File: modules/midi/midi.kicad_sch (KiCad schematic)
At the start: 9 parts, among them J2 GATE_OUTS, J3 AudioJack3, J4 CONFIG

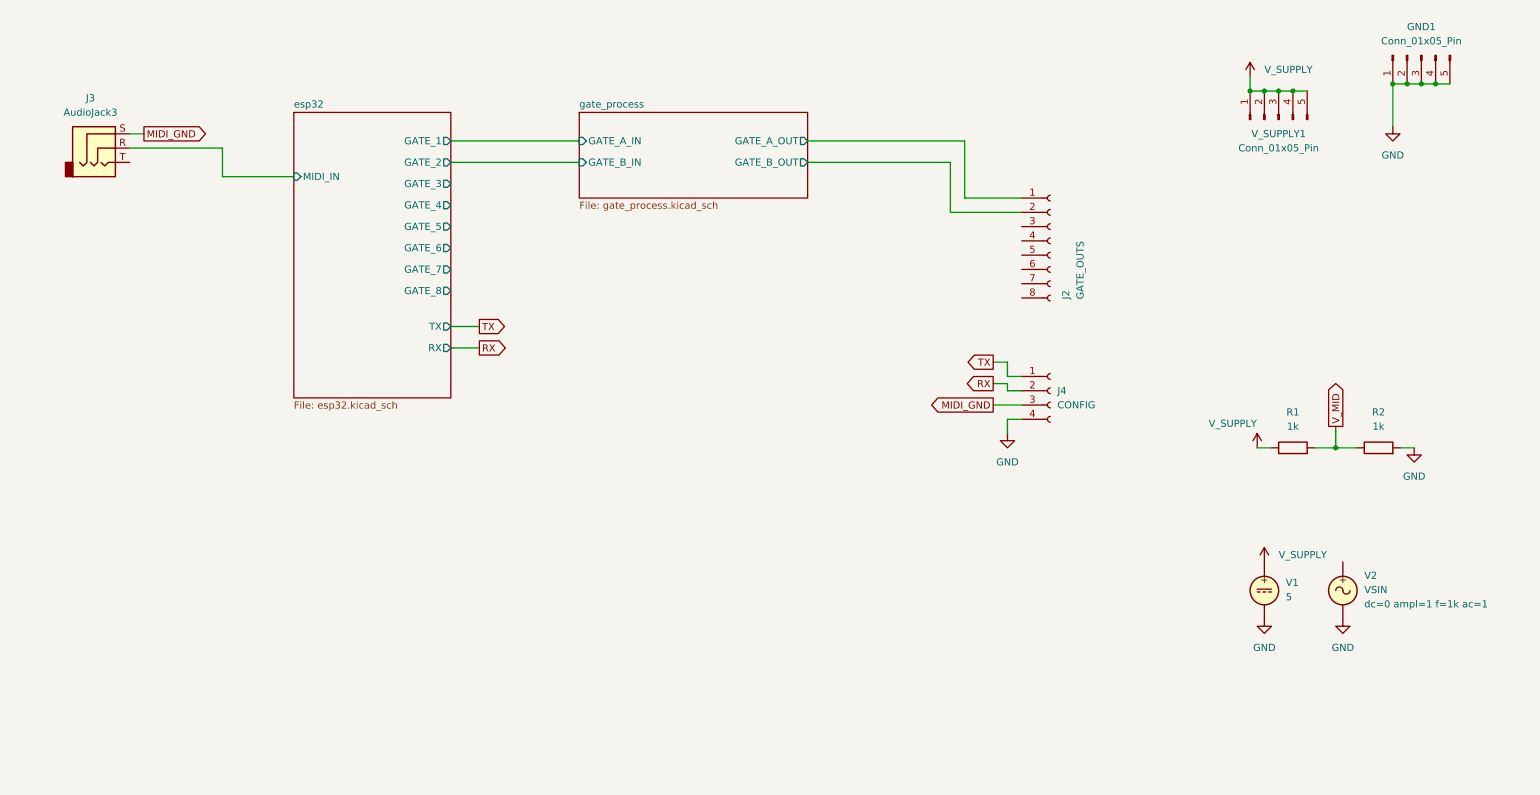
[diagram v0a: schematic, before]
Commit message: Add MIDI PCB
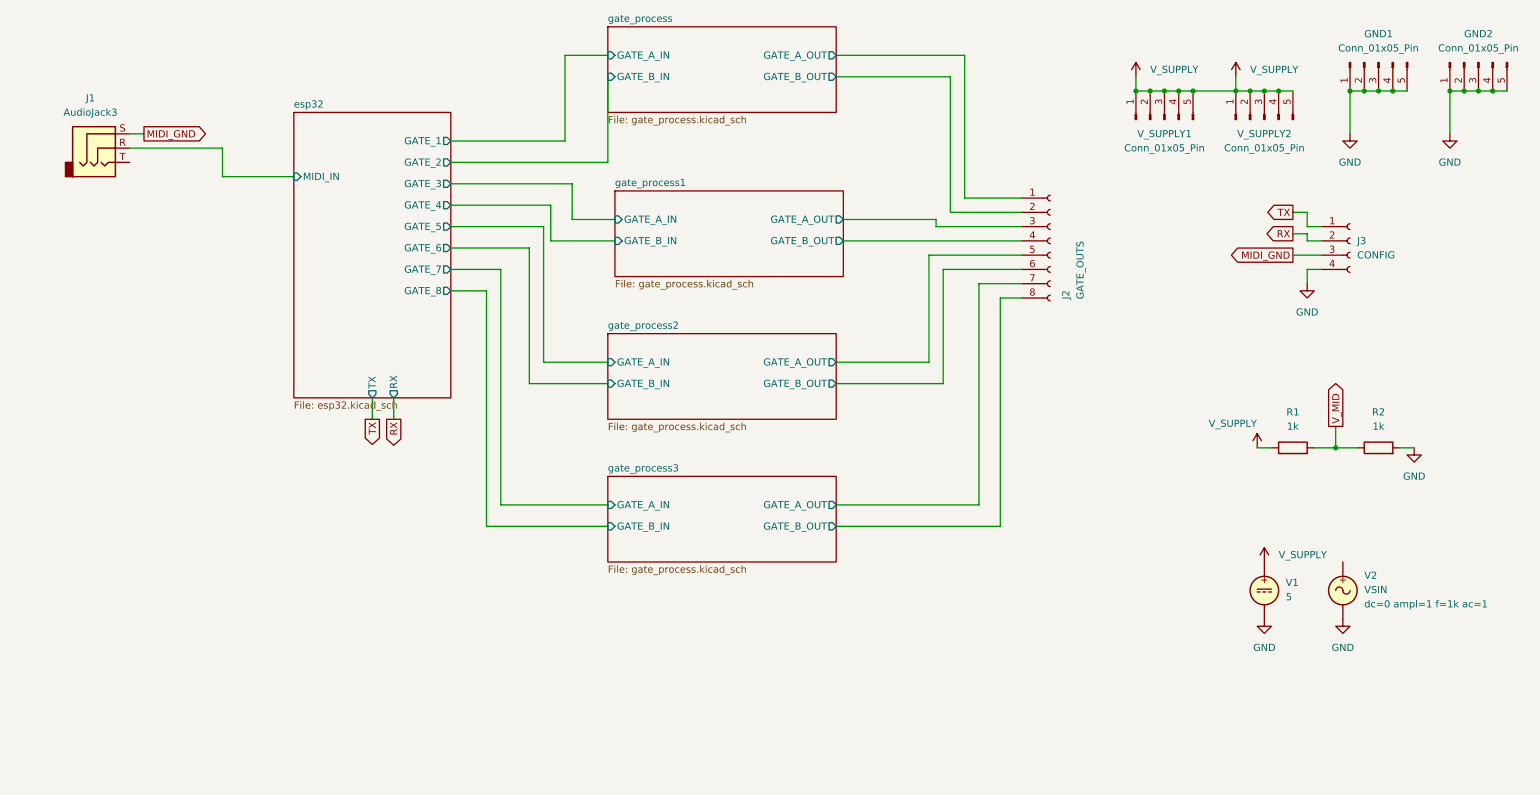
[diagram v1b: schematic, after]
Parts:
- added GND2, V_SUPPLY2: Conn_01x05_Pin, BreadModular_MISC:Power_Connector, symbol Connector:Conn_01x05_Pin
- renumbered J3 to J1, J4 to J3
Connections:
- net GND: now also GND2.1 (Pin_1), GND2.2 (Pin_2), GND2.3 (Pin_3), GND2.4 (Pin_4), GND2.5 (Pin_5)
- net V_SUPPLY: now also V_SUPPLY2.1 (Pin_1), V_SUPPLY2.2 (Pin_2), V_SUPPLY2.3 (Pin_3), V_SUPPLY2.4 (Pin_4), V_SUPPLY2.5 (Pin_5)
- net gate_process1/GATE_A_OUT: now reaches J2.3 (Pin_3)
- net gate_process1/GATE_B_OUT: now reaches J2.4 (Pin_4)
- net gate_process2/GATE_A_OUT: now reaches J2.5 (Pin_5)
- net gate_process2/GATE_B_OUT: now reaches J2.6 (Pin_6)
- net gate_process3/GATE_A_OUT: now reaches J2.7 (Pin_7)
- net gate_process3/GATE_B_OUT: now reaches J2.8 (Pin_8)
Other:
- added sheet gate_process1 (gate_process.kicad_sch)
- added sheet gate_process2 (gate_process.kicad_sch)
- added sheet gate_process3 (gate_process.kicad_sch)
- moved on the sheet: GND1, J3, V_SUPPLY1

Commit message: Implement the PCB layout and routing
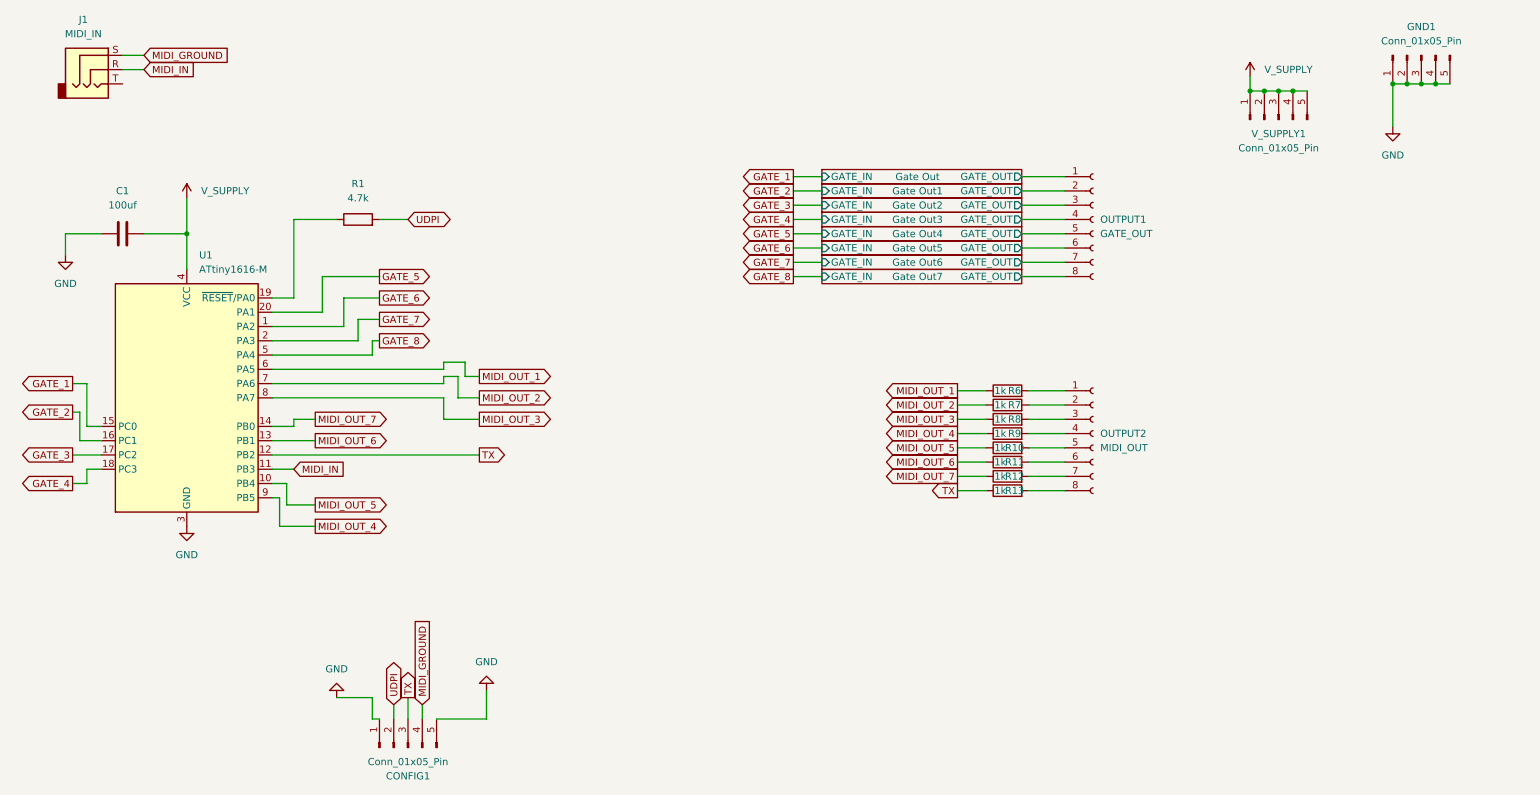
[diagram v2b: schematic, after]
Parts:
- removed GND2, V_SUPPLY2: Conn_01x05_Pin, BreadModular_MISC:Power_Connector, symbol Connector:Conn_01x05_Pin
- removed J2: GATE_OUTS, Connector_PinSocket_2.54mm:PinSocket_1x08_P2.54mm_Vertical, symbol Connector:Conn_01x08_Socket
- removed J3: CONFIG, Connector_PinSocket_2.54mm:PinSocket_1x04_P2.54mm_Vertical, symbol Connector:Conn_01x04_Socket
- removed R2: 1k, Resistor_SMD:R_0402_1005Metric, symbol Device:R
- removed V1: 5, symbol Simulation_SPICE:VDC
- removed V2: VSIN, symbol Simulation_SPICE:VSIN
- added C1: 100uf, Capacitor_SMD:C_1206_3216Metric, symbol Device:C
- added CONFIG1: Conn_01x05_Pin, BreadModular_MISC:Power_Connector, symbol Connector:Conn_01x05_Pin
- added OUTPUT1: GATE_OUT, Connector_PinSocket_2.54mm:PinSocket_1x08_P2.54mm_Vertical, symbol Connector:Conn_01x08_Socket
- added OUTPUT2: MIDI_OUT, Connector_PinSocket_2.54mm:PinSocket_1x08_P2.54mm_Vertical, symbol Connector:Conn_01x08_Socket
- added R10, R11, R12, R13, R6, R7, R8, R9: 1k, Resistor_SMD:R_0402_1005Metric, symbol Device:R
- added U1: ATtiny1616-M, Package_DFN_QFN:VQFN-20-1EP_3x3mm_P0.4mm_EP1.7x1.7mm, symbol MCU_Microchip_ATtiny:ATtiny1616-M
- J1: value AudioJack3 -> MIDI_IN
- R1: value 1k -> 4.7k
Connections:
- net GND: now also C1.1, CONFIG1.1 (Pin_1), CONFIG1.5 (Pin_5), U1.21 (GND), U1.3 (GND)
- net TX: now also CONFIG1.3 (Pin_3), R13.1, U1.12 (PB2)
- net V_SUPPLY: now also C1.2, U1.4 (VCC); no longer R1.1
- net MIDI_GND renamed MIDI_GROUND
- net MIDI_GROUND: now also CONFIG1.4 (Pin_4)
- net V_MID renamed UDPI
- net UDPI: now also CONFIG1.2 (Pin_2)
- net esp32/MIDI_IN renamed MIDI_IN
- net MIDI_IN: now also U1.11 (PB3)
- new net: OUTPUT2.1 (Pin_1), R6.2
- new net: OUTPUT2.2 (Pin_2), R7.2
- new net: OUTPUT2.3 (Pin_3), R8.2
- new net: OUTPUT2.4 (Pin_4), R9.2
- new net: OUTPUT2.5 (Pin_5), R10.2
- new net: OUTPUT2.6 (Pin_6), R11.2
- new net: OUTPUT2.7 (Pin_7), R12.2
- new net: OUTPUT2.8 (Pin_8), R13.2
- new net: R1.1, U1.19 (~{RESET}/PA0)
- new net GATE_1: U1.15 (PC0)
- new net GATE_2: U1.16 (PC1)
- new net GATE_3: U1.17 (PC2)
- new net GATE_4: U1.18 (PC3)
- new net GATE_5: U1.20 (PA1)
- new net GATE_6: U1.1 (PA2)
- new net GATE_7: U1.2 (PA3)
- new net GATE_8: U1.5 (PA4)
- new net Gate Out/GATE_OUT: OUTPUT1.1 (Pin_1)
- new net Gate Out1/GATE_OUT: OUTPUT1.2 (Pin_2)
- new net Gate Out2/GATE_OUT: OUTPUT1.3 (Pin_3)
- new net Gate Out3/GATE_OUT: OUTPUT1.4 (Pin_4)
- new net Gate Out4/GATE_OUT: OUTPUT1.5 (Pin_5)
- new net Gate Out5/GATE_OUT: OUTPUT1.6 (Pin_6)
- new net Gate Out6/GATE_OUT: OUTPUT1.7 (Pin_7)
- new net Gate Out7/GATE_OUT: OUTPUT1.8 (Pin_8)
- new net MIDI_OUT_1: R6.1, U1.6 (PA5)
- new net MIDI_OUT_2: R7.1, U1.7 (PA6)
- new net MIDI_OUT_3: R8.1, U1.8 (PA7)
- new net MIDI_OUT_4: R9.1, U1.9 (PB5)
- new net MIDI_OUT_5: R10.1, U1.10 (PB4)
- new net MIDI_OUT_6: R11.1, U1.13 (PB1)
- new net MIDI_OUT_7: R12.1, U1.14 (PB0)
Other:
- removed sheet esp32
- removed sheet gate_process
- removed sheet gate_process1
- removed sheet gate_process2
- removed sheet gate_process3
- added sheet Gate Out (gate_out.kicad_sch)
- added sheet Gate Out1 (gate_out.kicad_sch)
- added sheet Gate Out2 (gate_out.kicad_sch)
- added sheet Gate Out3 (gate_out.kicad_sch)
- added sheet Gate Out4 (gate_out.kicad_sch)
- added sheet Gate Out5 (gate_out.kicad_sch)
- added sheet Gate Out6 (gate_out.kicad_sch)
- added sheet Gate Out7 (gate_out.kicad_sch)
- moved on the sheet: GND1, V_SUPPLY1

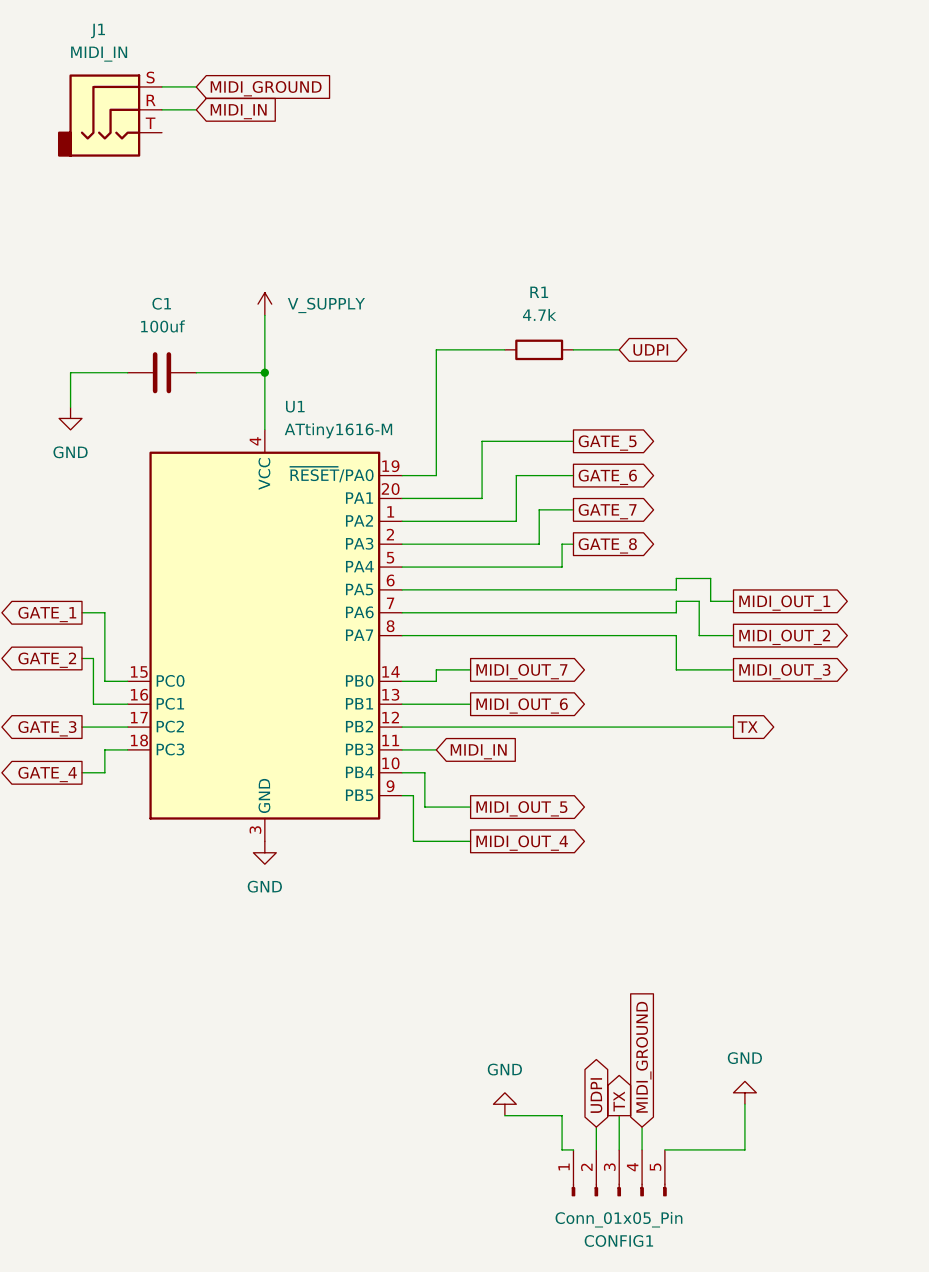
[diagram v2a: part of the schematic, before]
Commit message: midi: Add support to select MIDI A or B
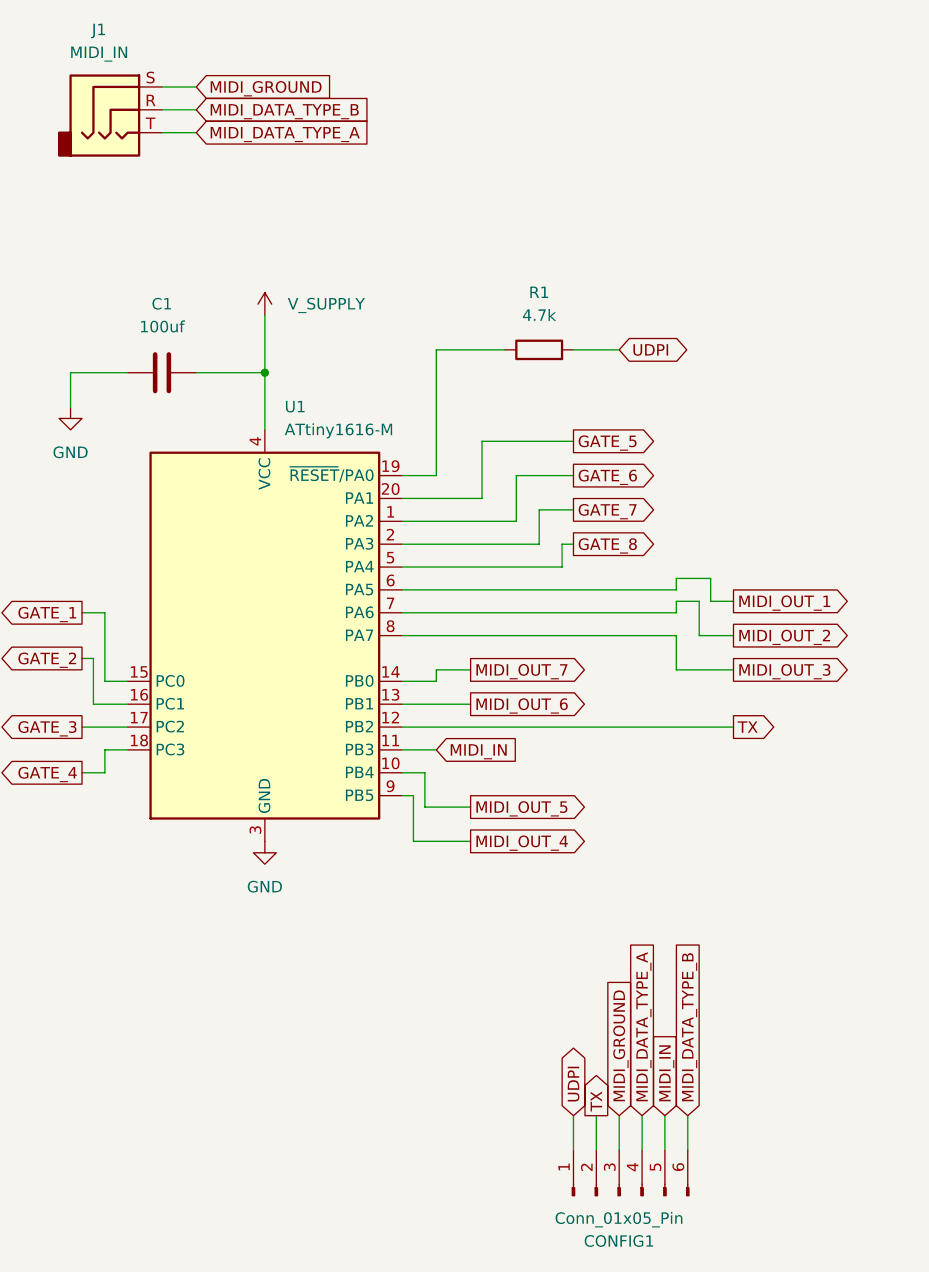
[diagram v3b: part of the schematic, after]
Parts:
- CONFIG1: footprint BreadModular_MISC:Power_Connector -> BreadModular_MISC:Conn_Holes_6; symbol Connector:Conn_01x05_Pin -> Connector:Conn_01x06_Pin
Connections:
- net GND: no longer CONFIG1.1 (Pin_1), CONFIG1.5 (Pin_5)
- net MIDI_GROUND: now also CONFIG1.3 (Pin_3); no longer CONFIG1.4 (Pin_4)
- net MIDI_IN: now also CONFIG1.5 (Pin_5); no longer J1.R
- net TX: now also CONFIG1.2 (Pin_2); no longer CONFIG1.3 (Pin_3)
- net UDPI: now also CONFIG1.1 (Pin_1); no longer CONFIG1.2 (Pin_2)
- net MIDI_DATA_TYPE_A: now reaches J1.T
- net MIDI_DATA_TYPE_A: now also CONFIG1.4 (Pin_4)
- new net MIDI_DATA_TYPE_B: CONFIG1.6 (Pin_6), J1.R
